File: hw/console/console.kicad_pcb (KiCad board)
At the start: 2 copper layers, 156 x 74 mm, 161 parts, among them J1 Batt, J301 USB-C 16P, J401 DM3AT-SF-PEJM5, J501 SPK 8R, J601 FFC-40 0.5mm, J901 UART, Q601 AO3400A, SW1 Движок, SW101 UP, SW102 DOWN, SW103 LEFT, SW104 RIGHT, SW105 SELECT, SW106 START, SW107 A, SW108 B, SW109 C, SW110 D, U1 F133-A, U2 SY8089AAAC, U3 SY8089AAAC, U4 SY8089AAAC, U401 W25Q32JVSSIQ, U5 TP4056, U501 PAM8301, Y1 24 МГц, Y2 32.768 кГц

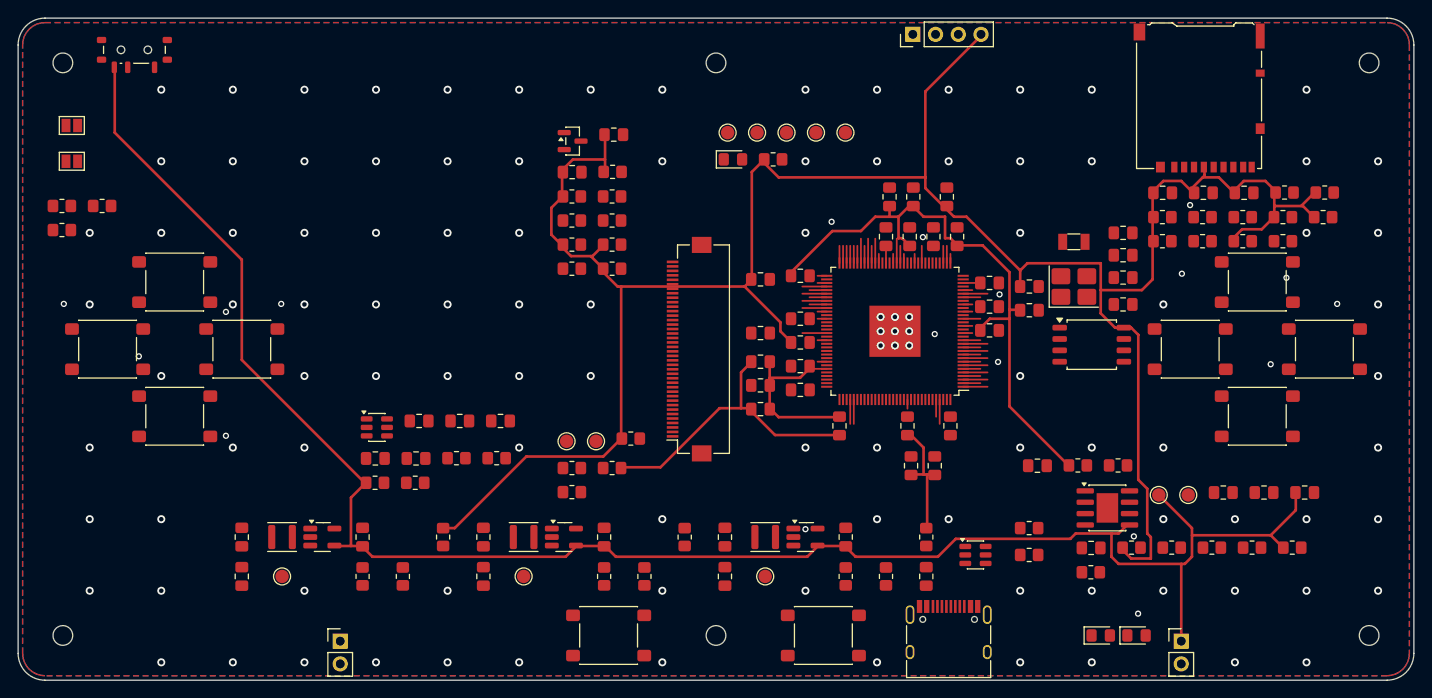
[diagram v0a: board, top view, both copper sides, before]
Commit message: hw: свой трассировщик ходил по кругу — не видел собственной вчерашней меди
Гонял его несколько заходов подряд: меди на плате стало вчетверо больше (1633
отрезка против 342), а неподключённых ровно столько же — 177. Причина простая
и стыдная: связное он начинает считать от первой площадки цепи, а уже
проложенные дорожки видит только как помеху. Каждый заход тянет вторую дорожку
от той же площадки рядом с первой.

Плата пересобрана начисто, одним проходом: 381 отрезок, 206 переходных, ноль
нарушений DRC, неподключённых 203.

Заодно цена изнанки приведена в чувство. Стояло `BACK_COST = 3` и
`VIA_COST = 25` — от замысла «изнанка сплошная земля», которого больше нет. С
такой ценой он не уходил на обратную сторону никогда: шесть переходных на всю
плату. Теперь 1.2 и 12, и обе стороны в работе. Бюджет поиска и число проходов
вынесены в окружение: кусту питания нужен щедрый, сотне коротких сигналов
дешевле быстро сдаться.

Co-Authored-By: Claude Opus 5 <noreply@anthropic.com>
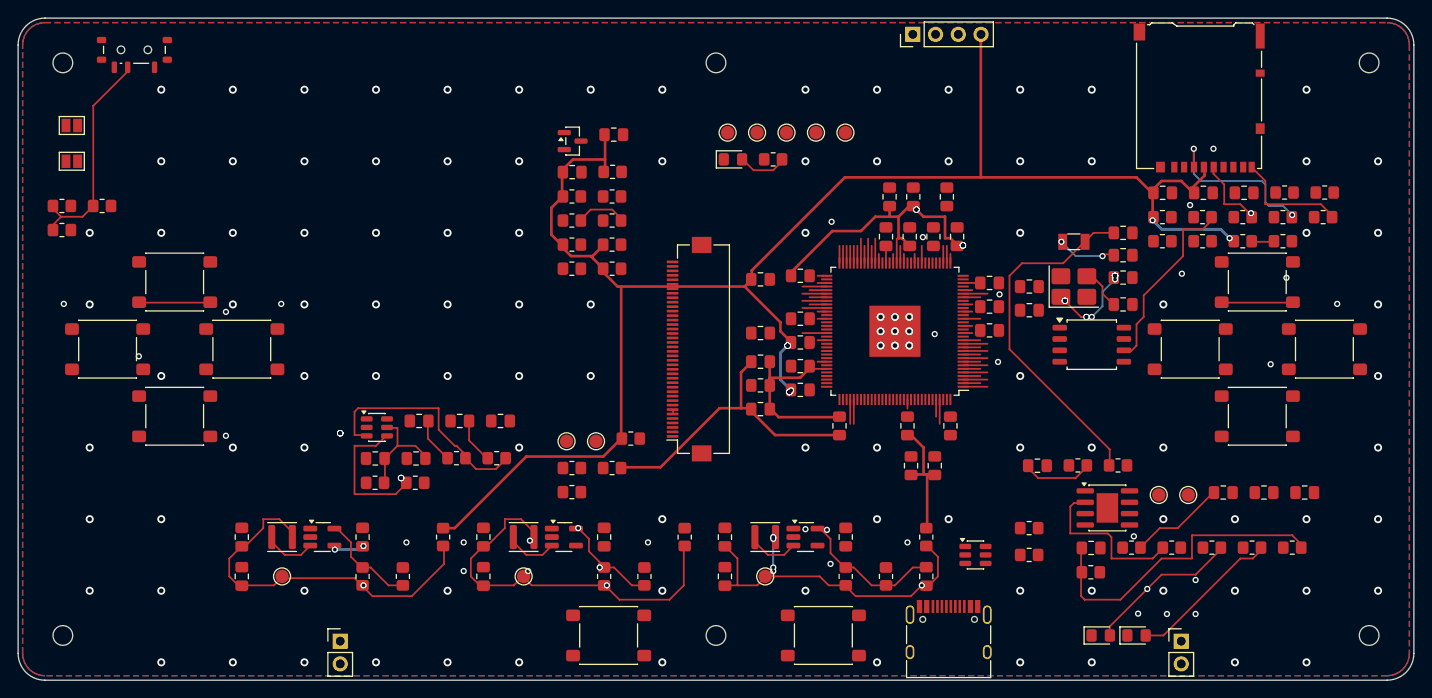
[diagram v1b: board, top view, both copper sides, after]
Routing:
- net VSYS: track 204.8 -> 3.97 mm, vias 1 -> 3
- net +3V3: track 266.9 -> 192.3 mm, vias 0 -> 14
- net Net-(C5-Pad1): track 0.00 -> 43.4 mm, vias 0 -> 6
- net Net-(C4-Pad1): track 0.00 -> 41.9 mm, vias 0 -> 2
- net Net-(C10-Pad1): track 0.00 -> 39.5 mm, vias 0 -> 6
- net X32KOUT: track 1.03 -> 40.5 mm
- net +1V8: track 75.6 -> 39.0 mm, vias 0 -> 10
- net GPADC0: track 2.72 -> 38.2 mm
- net Net-(U501-IN): track 0.00 -> 26.0 mm
- net /PWR_EN: track 0.00 -> 24.7 mm
- net NOR-CLK: track 0.00 -> 20.8 mm
- net SDC0-CMD: track 1.93 -> 21.0 mm, vias 1 -> 3
- net Net-(U5-PROG): track 0.00 -> 18.2 mm
- net Net-(D2-A): track 0.00 -> 17.2 mm, vias 0 -> 2
- net Net-(D1-A): track 0.00 -> 17.2 mm, vias 0 -> 2
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
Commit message: hw: трассировщик видит свою прежнюю медь соединённой
Продолжение вчерашней находки. Заход по остатку: 133 связи «проложено», а на
плату легло тридцать отрезков — остальные и правда уже были соединены, просто
раньше он этого не знал и тянул рядом вторую дорожку. Дублирования больше нет,
заходы стали добивать остаток, а не наращивать медь.

Неподключённых 197 при нуле нарушений DRC.

Co-Authored-By: Claude Opus 5 <noreply@anthropic.com>
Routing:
- net +3V3: track 192.3 -> 229.0 mm, vias 14 -> 16
- net SPI0-MISO: track 3.62 -> 34.0 mm
- net +1V8: track 39.0 -> 40.4 mm

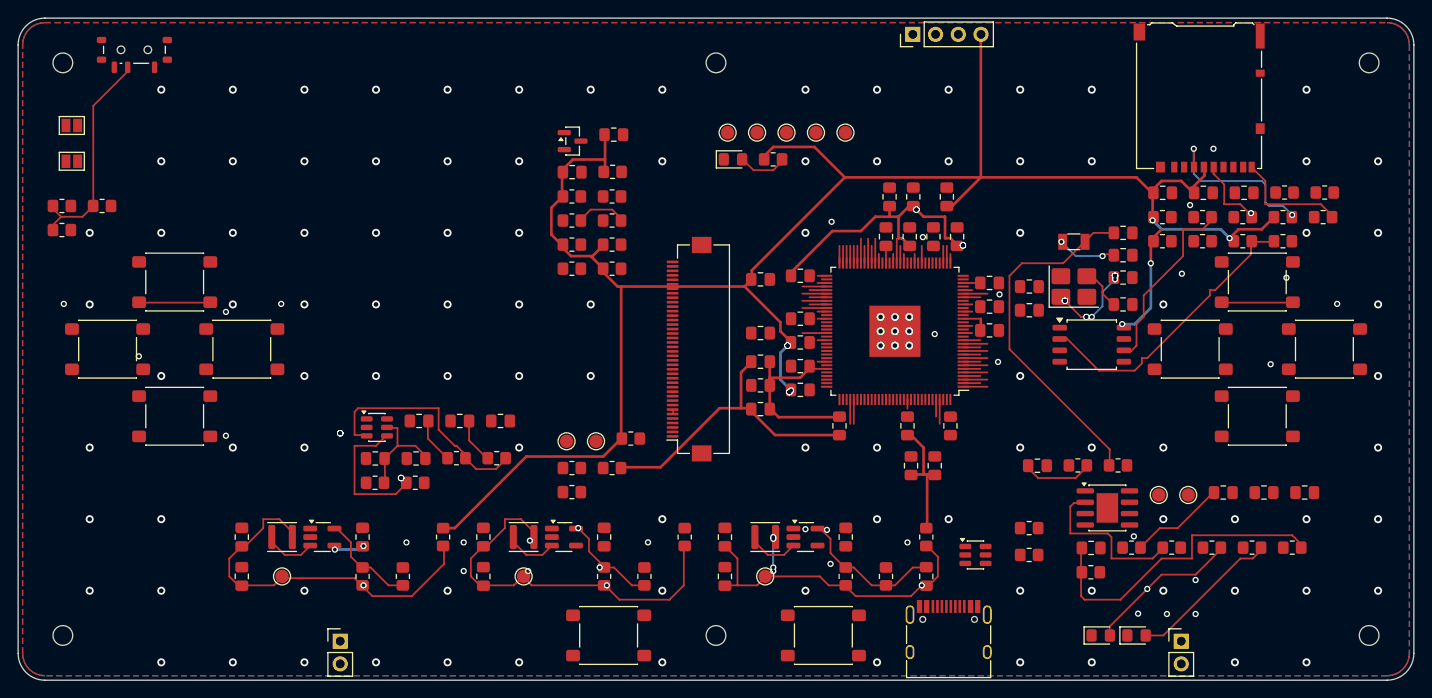
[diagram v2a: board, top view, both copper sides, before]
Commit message: hw: посадочные места HandSolder были стеной для веера, а сшивка портила замеры
Спросил двоих со стороны, и оба нашли то, чего я не видел.

**Стена оказалась в футпринтах.** Кольцо развязки стоит вплотную к выводам —
так и задумано, — а `C_0805_..._HandSolder` добавляет по 0.29 мм на сторону, и
вся эта прибавка приходится ровно туда, где сигналам выходить. Слева от
корпуса свободный ход был 0.40 мм у всех 32 выводов, то есть стена. Штатный
`C_0805_2012Metric` (паяем феном, `HandSolder` придуман под паяльник):
**веер выходит целиком, 90 сигналов из 90 вместо 65.**

**Замурован не только чип.** У разъёма шлейфа 26 площадок из 31 и у розетки
USB-C все 10 — тот же счёт: дорожка 0.2 с зазорами занимает 0.6 мм, при шаге
0.5 между площадками не пройти. До этих 36 площадок не дошёл бы никакой
трассировщик. Веер теперь и у них, всего 108 лучей.

**Свой трассировщик ускорен втрое** — `can_via` съедал две трети времени,
пересчитываясь для одной клетки до девяти раз, потому что направление входило
в состояние поиска. Мемоизация и состояние без направления: питание
разводится за восемь секунд вместо четырёх минут, вся плата — за минуту.

**И почему замеры плясали.** `pcb07_fanout.py` снимал дорожки, но не
переходные, а сшивка земли от прошлого круга ставится по свободному полю, то
есть каждый раз иначе. Один и тот же прогон давал то 177 несошедшихся связей,
то 206 — разница была не в том, что я правил, а в том, где вчера легли
заклёпки.

Ещё: переходная теперь занимает своё место в модели (без этого соседняя
дорожка ложилась к ней вплотную), а габарит площадки раздут на полклетки —
сетка ложится как придётся, и округление срезало до 0.025 мм зазора.

Итог: 144 неподключённых против 197, ноль нарушений DRC, прогон воспроизводим.

Трёх радиусов у веера не делаем, хотя расчёт за них: померено, с ними хуже
(195 против 177) — лучи съедают то самое место у корпуса, ради которого всё
и затевалось.

Co-Authored-By: Claude Opus 5 <noreply@anthropic.com>
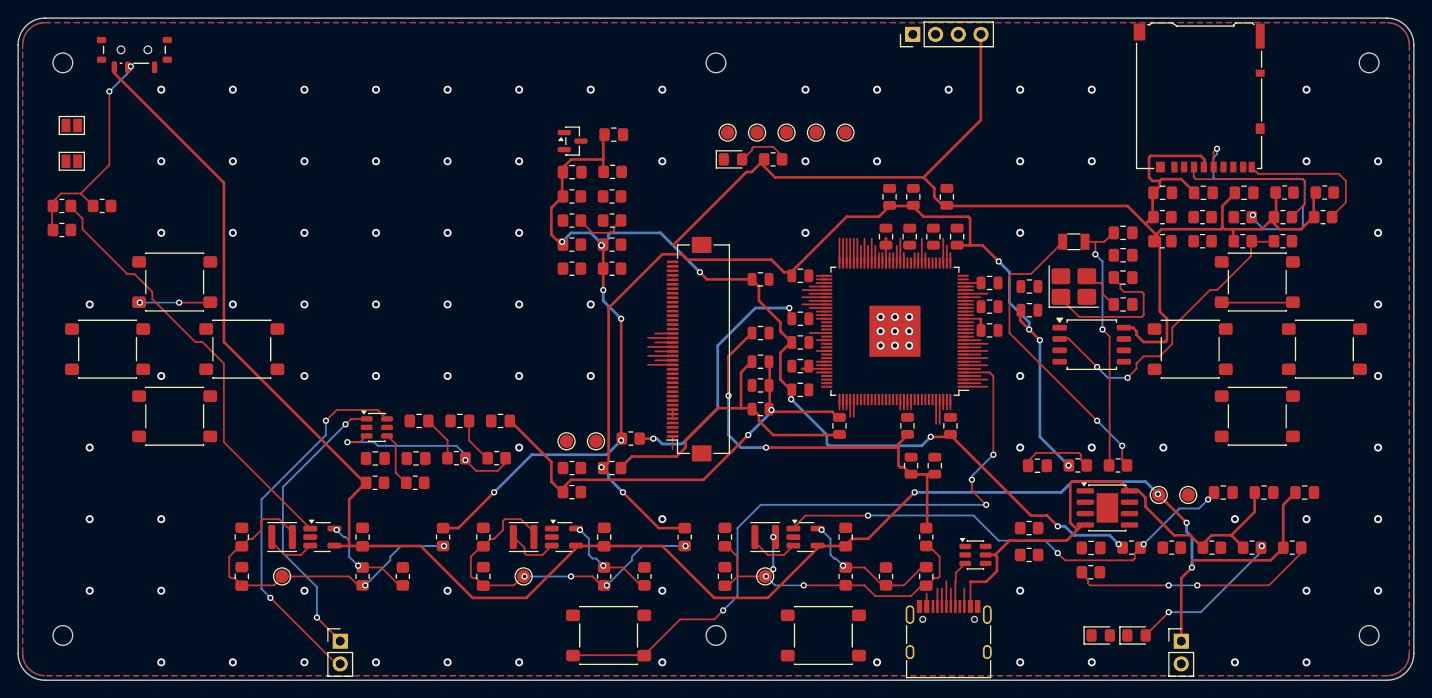
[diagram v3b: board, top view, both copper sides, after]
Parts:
- C801, C802, C803, C804, C805, C806, C807, C808, C809, C810, C811, C812, C813, C814, C815, C816, C817, C818, C819, C820, C821, C822, C823, C824, C825, C826, C827: footprint Capacitor_SMD:C_0805_2012Metric_Pad1.18x1.45mm_HandSolder -> Capacitor_SMD:C_0805_2012Metric
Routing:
- net VSYS: track 3.97 -> 207.4 mm, vias 3 -> 4
- net +1V8: track 40.4 -> 125.8 mm, vias 10 -> 6
- net +3V3: track 229.0 -> 311.5 mm, vias 16 -> 12
- net KEY-SELECT: track 2.72 -> 77.2 mm, vias 0 -> 4
- net VBUS: track 0.00 -> 57.9 mm
- net EN_3V3: track 0.00 -> 48.0 mm, vias 2 -> 0
- net EN_0V9: track 10.8 -> 53.3 mm, vias 2 -> 4
- net Net-(J501-Pin_2): track 0.00 -> 41.8 mm, vias 0 -> 2
- net +0V9: track 20.7 -> 55.1 mm, vias 0 -> 2
- net AGND: track 20.6 -> 54.9 mm, vias 0 -> 2
- net Net-(J501-Pin_1): track 0.00 -> 32.4 mm, vias 0 -> 2
- net VCC-TVOUT: track 1.03 -> 29.9 mm, vias 0 -> 2
- net X32KIN: track 6.75 -> 35.4 mm
- net NOR-CLK: track 20.8 -> 0.00 mm
- net SD-CLK: track 8.39 -> 28.0 mm
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
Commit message: hw: сетка сшивки 12.7 вместо 8 — заклёпок 39 вместо 94
Каждая заклёпка это два сверления и пайка проволочки с обеих сторон, то есть
шаг сетки — прямая цена работы. Стояло 8 мм «с запасом», и выходило 94 штуки:
больше, чем вся разводка платы.

Посчитано по делу: наружу у нас ничего быстрее шины дисплея не выходит (ядро
480 МГц и DDR заперты внутри корпуса), f_knee порядка 400 МГц, λ/20 ≈ 21 мм.
TI SZZA009 и Отт для двухслойных плат дают 12.7 мм.

Всего переходных на плате 111 вместо 166. Разводка и DRC не пострадали.

Co-Authored-By: Claude Opus 5 <noreply@anthropic.com>
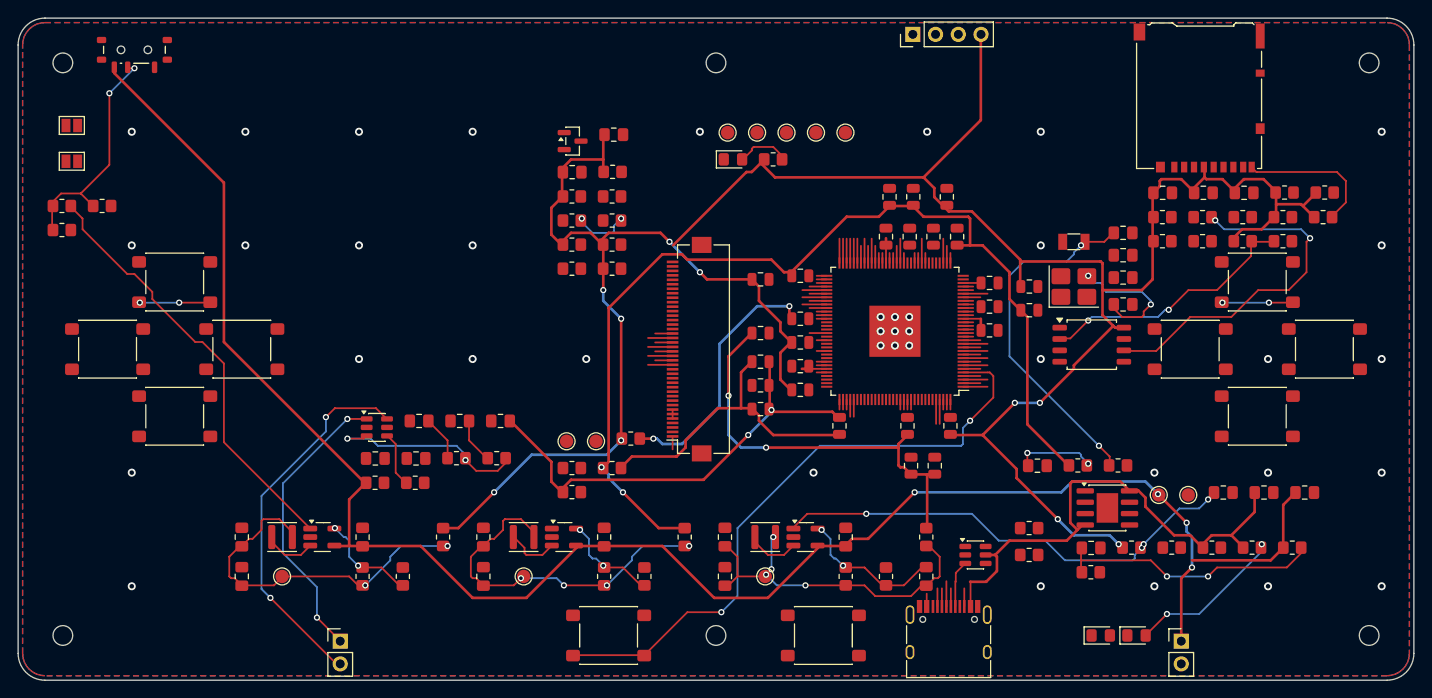
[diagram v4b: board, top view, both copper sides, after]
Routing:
- net NOR-CLK: track 0.00 -> 40.0 mm, vias 0 -> 2
- net X32KIN: track 35.4 -> 1.12 mm, vias 2 -> 0
- net SD-CLK: track 28.0 -> 0.00 mm, vias 2 -> 0
- net SDC0-CMD: track 20.3 -> 1.93 mm
- net DXOUT: track 18.2 -> 1.12 mm
- net +3V3: track 311.5 -> 296.8 mm, vias 12 -> 10
- net X32KOUT: track 30.4 -> 40.7 mm
- net DXIN: track 6.04 -> 15.9 mm, vias 0 -> 2
- net KEY-SELECT: track 77.2 -> 70.3 mm, vias 4 -> 2
- net SPI0-MISO: track 35.6 -> 30.5 mm
- net +1V8: track 125.8 -> 123.2 mm, vias 6 -> 2
- net GPADC0: track 29.4 -> 31.7 mm
- net Net-(C5-Pad1): track 40.2 -> 41.1 mm
- net Net-(C4-Pad1): track 40.0 -> 40.8 mm
- net LCD-RS: track 5.99 -> 6.79 mm, vias 0 -> 2
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
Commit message: hw: трассировщик считал куски одной цепи соединённым целым
Он говорил «питание разведено, шесть неудач», а DRC показывал сорок разрывов
по тем же цепям. Причина: медь цепи бралась одним блобом. У `+3V3` тридцать
восемь площадок, дерево собрано наполовину, куски друг с другом не связаны — а
он видел сплошное «уже соединено» и не делал ничего.

Теперь связность считается по-настоящему: объединение-поиск по рёбрам «конец
дорожки — конец дорожки» и «лицо — изнанка в точке переходной», старт от того
куска, в котором лежит первая площадка.

Счёт стал честным и сошёлся с DRC: 147 неудач против 144 разрывов. Разведено
около 124 связей из 270 — это и видно в KiCad, я до сих пор докладывал лучше,
чем есть.

Co-Authored-By: Claude Opus 5 <noreply@anthropic.com>
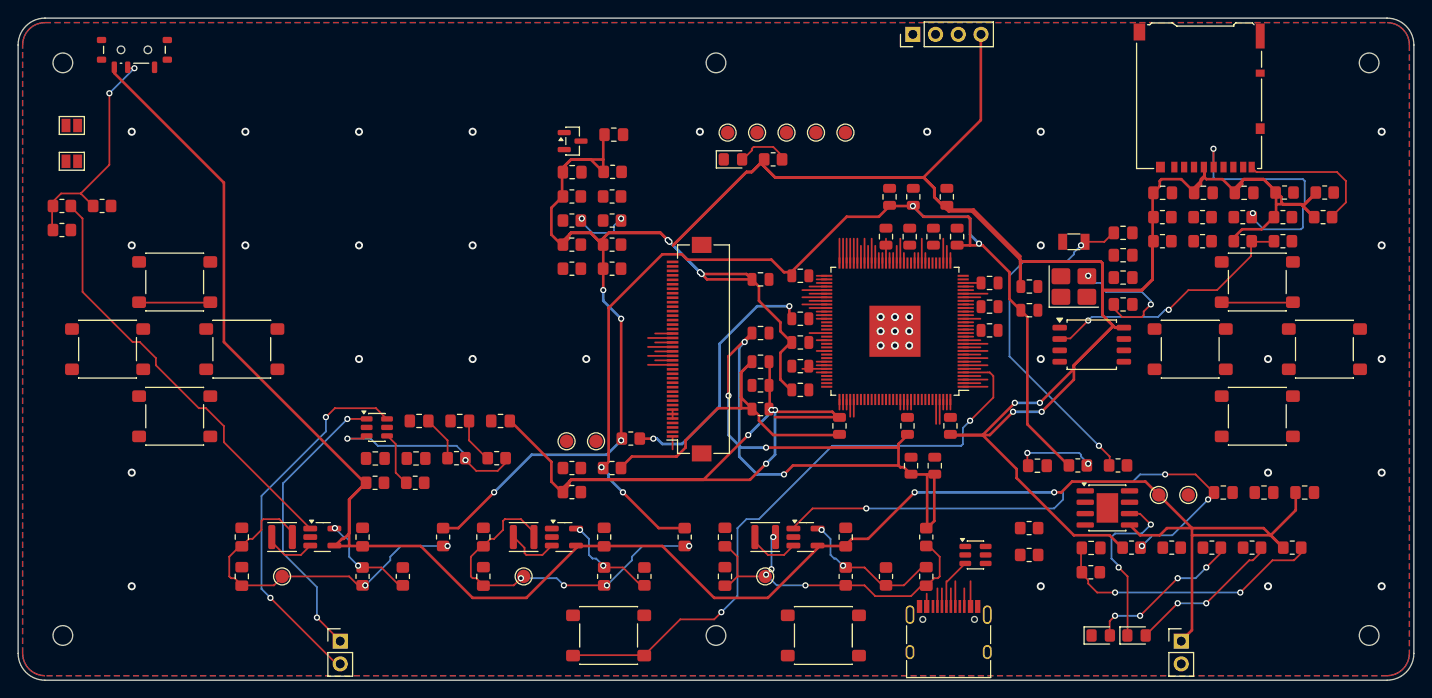
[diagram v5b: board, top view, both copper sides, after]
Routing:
- net +3V3: track 296.8 -> 449.9 mm, vias 10 -> 12
- net VBUS: track 57.9 -> 4.25 mm
- net NOR-CLK: track 40.0 -> 0.00 mm, vias 2 -> 0
- net +0V9: track 55.1 -> 94.1 mm, vias 2 -> 4
- net AGND: track 54.9 -> 92.6 mm, vias 2 -> 4
- net SD-CLK: track 0.00 -> 28.1 mm, vias 0 -> 2
- net VSYS: track 207.4 -> 234.0 mm, vias 4 -> 2
- net Net-(D2-K): track 0.00 -> 19.6 mm, vias 0 -> 2
- net Net-(D1-A): track 0.00 -> 17.7 mm, vias 0 -> 4
- net +1V8: track 123.2 -> 132.5 mm, vias 2 -> 4
- net EN_0V9: track 53.7 -> 61.8 mm
- net AVCC: track 37.1 -> 43.3 mm
- net GPADC0: track 31.7 -> 32.9 mm
- net Net-(D2-A): track 18.1 -> 17.3 mm
- net KEY-UP: vias 2 -> 0
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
